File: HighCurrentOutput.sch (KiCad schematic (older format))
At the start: 8 parts, among them J10 OUT 1, Q1 SISA88DN or similar

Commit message: preliminary placement done
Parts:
- J10: footprint Connector_Molex:Molex_Nano-Fit_105313-xx02_1x02_P2.50mm_Horizontal -> TXV_LIB:Molex_Nano-Fit_105313-xx02_1x02_P2.50mm_Horizontal
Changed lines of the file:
@@
 F 0 "J20" H 6105 3317 50  0000 L CNN
 F 1 "OUT 1" H 6105 3226 50  0000 L CNN
-F 2 "Connector_Molex:Molex_Nano-Fit_105313-xx02_1x02_P2.50mm_Horizontal" H 6025 3325 50  0001 C CNN
+F 2 "TXV_LIB:Molex_Nano-Fit_105313-xx02_1x02_P2.50mm_Horizontal" H 6025 3325 50  0001 C CNN
 F 3 "" H 6025 3325 50  0001 C CNN
 F 4 "" H 6025 3325 50  0001 C CNN "Male Mate"

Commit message: changed form factor to better fit into uHb engine section
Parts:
- J10: footprint TXV_LIB:Molex_Nano-Fit_105313-xx02_1x02_P2.50mm_Horizontal -> TXV_LIB:Molex_Nano-Fit_105309-xx02_1x02_P2.50mm_Vertical
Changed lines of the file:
@@
 F 0 "J20" H 6105 3317 50  0000 L CNN
 F 1 "OUT 1" H 6105 3226 50  0000 L CNN
-F 2 "TXV_LIB:Molex_Nano-Fit_105313-xx02_1x02_P2.50mm_Horizontal" H 6025 3325 50  0001 C CNN
+F 2 "TXV_LIB:Molex_Nano-Fit_105309-xx02_1x02_P2.50mm_Vertical" H 6025 3325 50  0001 C CNN
 F 3 "" H 6025 3325 50  0001 C CNN
 F 4 "" H 6025 3325 50  0001 C CNN "Male Mate"

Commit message: many small changes, before removing servo buck converter
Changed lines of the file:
@@
 AR Path="/636FF559/637A9A68" Ref="J10"  Part="1"
 AR Path="/64079439/637A9A68" Ref="J20"  Part="1"
-F 0 "J20" H 6105 3317 50  0000 L CNN
+F 0 "J10" H 6105 3317 50  0000 L CNN
 F 1 "OUT 1" H 6105 3226 50  0000 L CNN
 F 2 "TXV_LIB:Molex_Nano-Fit_105309-xx02_1x02_P2.50mm_Vertical" H 6025 3325 50  0001 C CNN
@@
 AR Path="/636FF559/637A9A72" Ref="#PWR0119"  Part="1"
 AR Path="/64079439/637A9A72" Ref="#PWR0176"  Part="1"
-F 0 "#PWR0176" H 5800 3075 50  0001 C CNN
+F 0 "#PWR0119" H 5800 3075 50  0001 C CNN
 F 1 "+12V" H 5800 3375 50  0000 C CNN
 F 2 "" H 5800 3225 50  0001 C CNN
@@
 AR Path="/636FF559/637A9A79" Ref="D7"  Part="1"
 AR Path="/64079439/637A9A79" Ref="D10"  Part="1"
-F 0 "D10" V 5650 3575 50  0000 R CNN
+F 0 "D7" V 5650 3575 50  0000 R CNN
 F 1 "Shottky" V 5725 3700 50  0000 R CNN
 F 2 "Diode_SMD:D_SOD-123F" V 5700 3375 50  0001 C CNN
@@
 AR Path="/636FF559/637A9A88" Ref="R29"  Part="1"
 AR Path="/64079439/637A9A88" Ref="R58"  Part="1"
-F 0 "R58" H 5175 3825 50  0000 R CNN
+F 0 "R29" H 5175 3825 50  0000 R CNN
 F 1 "9k1" H 5175 3900 50  0000 R CNN
 F 2 "Resistor_SMD:R_0603_1608Metric" H 5225 3850 50  0001 C CNN
@@
 AR Path="/636FF559/637A9A8F" Ref="#PWR0120"  Part="1"
 AR Path="/64079439/637A9A8F" Ref="#PWR0177"  Part="1"
-F 0 "#PWR0177" H 5800 3950 50  0001 C CNN
+F 0 "#PWR0120" H 5800 3950 50  0001 C CNN
 F 1 "GND" H 5800 4050 50  0000 C CNN
 F 2 "" H 5800 4200 50  0001 C CNN
@@
 AR Path="/636FF559/637A9A95" Ref="R30"  Part="1"
 AR Path="/64079439/637A9A95" Ref="R59"  Part="1"
-F 0 "R59" V 5525 3725 50  0000 C CNN
+F 0 "R30" V 5525 3725 50  0000 C CNN
 F 1 "120" V 5450 3725 50  0000 C CNN
 F 2 "Resistor_SMD:R_0603_1608Metric" H 5375 3725 50  0001 C CNN
@@
 AR Path="/636FF559/637A9A9F" Ref="R31"  Part="1"
 AR Path="/64079439/637A9A9F" Ref="R60"  Part="1"
-F 0 "R60" H 5600 4125 50  0000 L CNN
+F 0 "R31" H 5600 4125 50  0000 L CNN
 F 1 "10m 1W" H 5450 4025 50  0000 L CNN
 F 2 "Resistor_SMD:R_1206_3216Metric" H 5800 4075 50  0001 C CNN
@@
 AR Path="/636FF559/637A9AAA" Ref="D6"  Part="1"
 AR Path="/64079439/637A9AAA" Ref="D9"  Part="1"
-F 0 "D9" V 5100 4275 50  0000 R CNN
+F 0 "D6" V 5100 4275 50  0000 R CNN
 F 1 "OUT 1" V 5025 4375 50  0000 R CNN
 F 2 "LED_SMD:LED_0603_1608Metric" V 5075 4075 50  0001 C CNN
@@
 AR Path="/636FF559/637A9AB0" Ref="#PWR0121"  Part="1"
 AR Path="/64079439/637A9AB0" Ref="#PWR0178"  Part="1"
-F 0 "#PWR0178" H 5075 3950 50  0001 C CNN
+F 0 "#PWR0121" H 5075 3950 50  0001 C CNN
 F 1 "GND" H 5075 4050 50  0000 C CNN
 F 2 "" H 5075 4200 50  0001 C CNN
@@
 AR Path="/636FF559/637A9ABC" Ref="#PWR0122"  Part="1"
 AR Path="/64079439/637A9ABC" Ref="#PWR0179"  Part="1"
-F 0 "#PWR0179" H 5225 3725 50  0001 C CNN
+F 0 "#PWR0122" H 5225 3725 50  0001 C CNN
 F 1 "GND" H 5225 3825 50  0000 C CNN
 F 2 "" H 5225 3975 50  0001 C CNN
@@
 AR Path="/636FF559/637A9AC2" Ref="R28"  Part="1"
 AR Path="/64079439/637A9AC2" Ref="R57"  Part="1"
-F 0 "R57" H 4950 3875 50  0000 C CNN
+F 0 "R28" H 4950 3875 50  0000 C CNN
 F 1 "120" H 4950 3800 50  0000 C CNN
 F 2 "Resistor_SMD:R_0603_1608Metric" H 5075 3850 50  0001 C CNN
@@
 AR Path="/636FF559/637A9AC9" Ref="Q1"  Part="1"
 AR Path="/64079439/637A9AC9" Ref="Q2"  Part="1"
-F 0 "Q2" H 5905 3771 50  0000 L CNN
+F 0 "Q1" H 5905 3771 50  0000 L CNN
 F 1 "SISA88DN or similar" H 5905 3680 50  0000 L CNN
 F 2 "TXV_LIB:PowerPAK_1212-8" H 5900 3825 50  0001 C CNN

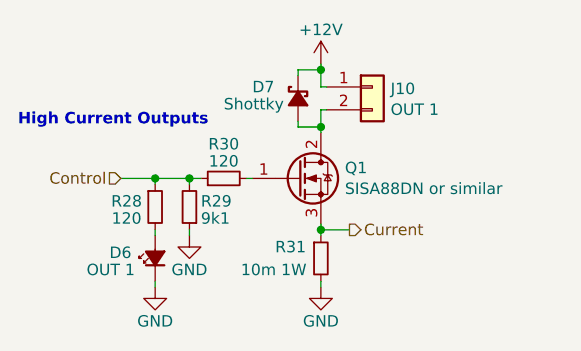
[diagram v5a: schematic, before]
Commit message: fixed net names
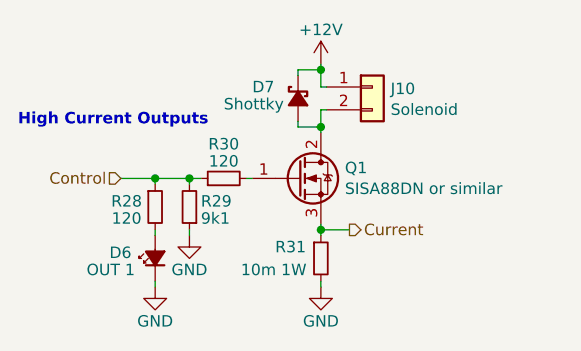
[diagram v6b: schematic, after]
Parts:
- J10: value OUT 1 -> Solenoid
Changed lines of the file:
@@
 AR Path="/64079439/637A9A68" Ref="J20"  Part="1"
 F 0 "J10" H 6105 3317 50  0000 L CNN
-F 1 "OUT 1" H 6105 3226 50  0000 L CNN
+F 1 "Solenoid" H 6105 3226 50  0000 L CNN
 F 2 "TXV_LIB:Molex_Nano-Fit_105309-xx02_1x02_P2.50mm_Vertical" H 6025 3325 50  0001 C CNN
 F 3 "" H 6025 3325 50  0001 C CNN
@@
 AR Path="/636FF559/637A9A72" Ref="#PWR0119"  Part="1"
 AR Path="/64079439/637A9A72" Ref="#PWR0176"  Part="1"
-F 0 "#PWR0119" H 5800 3075 50  0001 C CNN
+F 0 "#PWR0176" H 5800 3075 50  0001 C CNN
 F 1 "+12V" H 5800 3375 50  0000 C CNN
 F 2 "" H 5800 3225 50  0001 C CNN
@@
 AR Path="/636FF559/637A9A8F" Ref="#PWR0120"  Part="1"
 AR Path="/64079439/637A9A8F" Ref="#PWR0177"  Part="1"
-F 0 "#PWR0120" H 5800 3950 50  0001 C CNN
+F 0 "#PWR0177" H 5800 3950 50  0001 C CNN
 F 1 "GND" H 5800 4050 50  0000 C CNN
 F 2 "" H 5800 4200 50  0001 C CNN
@@
 AR Path="/636FF559/637A9AB0" Ref="#PWR0121"  Part="1"
 AR Path="/64079439/637A9AB0" Ref="#PWR0178"  Part="1"
-F 0 "#PWR0121" H 5075 3950 50  0001 C CNN
+F 0 "#PWR0178" H 5075 3950 50  0001 C CNN
 F 1 "GND" H 5075 4050 50  0000 C CNN
 F 2 "" H 5075 4200 50  0001 C CNN
@@
 AR Path="/636FF559/637A9ABC" Ref="#PWR0122"  Part="1"
 AR Path="/64079439/637A9ABC" Ref="#PWR0179"  Part="1"
-F 0 "#PWR0122" H 5225 3725 50  0001 C CNN
+F 0 "#PWR0179" H 5225 3725 50  0001 C CNN
 F 1 "GND" H 5225 3825 50  0000 C CNN
 F 2 "" H 5225 3975 50  0001 C CNN

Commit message: schematic done, preliminary placement done
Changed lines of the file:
@@
 $Descr A4 11693 8268
 encoding utf-8
-Sheet 5 18
+Sheet 13 18
 Title ""
 Date ""
@@
 AR Path="/636FF559/637A9A68" Ref="J10"  Part="1"
 AR Path="/64079439/637A9A68" Ref="J20"  Part="1"
-F 0 "J10" H 6105 3317 50  0000 L CNN
+F 0 "J20" H 6105 3317 50  0000 L CNN
 F 1 "Solenoid" H 6105 3226 50  0000 L CNN
 F 2 "TXV_LIB:Molex_Nano-Fit_105309-xx02_1x02_P2.50mm_Vertical" H 6025 3325 50  0001 C CNN
@@
 AR Path="/636FF559/637A9A79" Ref="D7"  Part="1"
 AR Path="/64079439/637A9A79" Ref="D10"  Part="1"
-F 0 "D7" V 5650 3575 50  0000 R CNN
+F 0 "D10" V 5650 3575 50  0000 R CNN
 F 1 "Shottky" V 5725 3700 50  0000 R CNN
 F 2 "Diode_SMD:D_SOD-123F" V 5700 3375 50  0001 C CNN
@@
 AR Path="/636FF559/637A9A88" Ref="R29"  Part="1"
 AR Path="/64079439/637A9A88" Ref="R58"  Part="1"
-F 0 "R29" H 5175 3825 50  0000 R CNN
+F 0 "R58" H 5175 3825 50  0000 R CNN
 F 1 "9k1" H 5175 3900 50  0000 R CNN
 F 2 "Resistor_SMD:R_0603_1608Metric" H 5225 3850 50  0001 C CNN
@@
 AR Path="/636FF559/637A9A95" Ref="R30"  Part="1"
 AR Path="/64079439/637A9A95" Ref="R59"  Part="1"
-F 0 "R30" V 5525 3725 50  0000 C CNN
+F 0 "R59" V 5525 3725 50  0000 C CNN
 F 1 "120" V 5450 3725 50  0000 C CNN
 F 2 "Resistor_SMD:R_0603_1608Metric" H 5375 3725 50  0001 C CNN
@@
 AR Path="/636FF559/637A9A9F" Ref="R31"  Part="1"
 AR Path="/64079439/637A9A9F" Ref="R60"  Part="1"
-F 0 "R31" H 5600 4125 50  0000 L CNN
+F 0 "R60" H 5600 4125 50  0000 L CNN
 F 1 "10m 1W" H 5450 4025 50  0000 L CNN
 F 2 "Resistor_SMD:R_1206_3216Metric" H 5800 4075 50  0001 C CNN
@@
 AR Path="/636FF559/637A9AAA" Ref="D6"  Part="1"
 AR Path="/64079439/637A9AAA" Ref="D9"  Part="1"
-F 0 "D6" V 5100 4275 50  0000 R CNN
+F 0 "D9" V 5100 4275 50  0000 R CNN
 F 1 "OUT 1" V 5025 4375 50  0000 R CNN
 F 2 "LED_SMD:LED_0603_1608Metric" V 5075 4075 50  0001 C CNN
@@
 AR Path="/636FF559/637A9AC2" Ref="R28"  Part="1"
 AR Path="/64079439/637A9AC2" Ref="R57"  Part="1"
-F 0 "R28" H 4950 3875 50  0000 C CNN
+F 0 "R57" H 4950 3875 50  0000 C CNN
 F 1 "120" H 4950 3800 50  0000 C CNN
 F 2 "Resistor_SMD:R_0603_1608Metric" H 5075 3850 50  0001 C CNN
@@
 AR Path="/636FF559/637A9AC9" Ref="Q1"  Part="1"
 AR Path="/64079439/637A9AC9" Ref="Q2"  Part="1"
-F 0 "Q1" H 5905 3771 50  0000 L CNN
+F 0 "Q2" H 5905 3771 50  0000 L CNN
 F 1 "SISA88DN or similar" H 5905 3680 50  0000 L CNN
 F 2 "TXV_LIB:PowerPAK_1212-8" H 5900 3825 50  0001 C CNN

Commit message: some more small changes
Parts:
- R29: value 9k1 -> 10k
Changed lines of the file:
@@
 $Descr A4 11693 8268
 encoding utf-8
-Sheet 13 18
+Sheet 5 18
 Title ""
 Date ""
@@
 AR Path="/636FF559/637A9A68" Ref="J10"  Part="1"
 AR Path="/64079439/637A9A68" Ref="J20"  Part="1"
-F 0 "J20" H 6105 3317 50  0000 L CNN
+F 0 "J10" H 6105 3317 50  0000 L CNN
 F 1 "Solenoid" H 6105 3226 50  0000 L CNN
 F 2 "TXV_LIB:Molex_Nano-Fit_105309-xx02_1x02_P2.50mm_Vertical" H 6025 3325 50  0001 C CNN
@@
 AR Path="/636FF559/637A9A79" Ref="D7"  Part="1"
 AR Path="/64079439/637A9A79" Ref="D10"  Part="1"
-F 0 "D10" V 5650 3575 50  0000 R CNN
+F 0 "D7" V 5650 3575 50  0000 R CNN
 F 1 "Shottky" V 5725 3700 50  0000 R CNN
 F 2 "Diode_SMD:D_SOD-123F" V 5700 3375 50  0001 C CNN
@@
 AR Path="/636FF559/637A9A88" Ref="R29"  Part="1"
 AR Path="/64079439/637A9A88" Ref="R58"  Part="1"
-F 0 "R58" H 5175 3825 50  0000 R CNN
-F 1 "9k1" H 5175 3900 50  0000 R CNN
+F 0 "R29" H 5175 3825 50  0000 R CNN
+F 1 "10k" H 5175 3900 50  0000 R CNN
 F 2 "Resistor_SMD:R_0603_1608Metric" H 5225 3850 50  0001 C CNN
 F 3 "~" H 5225 3850 50  0001 C CNN
@@
 AR Path="/636FF559/637A9A95" Ref="R30"  Part="1"
 AR Path="/64079439/637A9A95" Ref="R59"  Part="1"
-F 0 "R59" V 5525 3725 50  0000 C CNN
+F 0 "R30" V 5525 3725 50  0000 C CNN
 F 1 "120" V 5450 3725 50  0000 C CNN
 F 2 "Resistor_SMD:R_0603_1608Metric" H 5375 3725 50  0001 C CNN
@@
 AR Path="/636FF559/637A9A9F" Ref="R31"  Part="1"
 AR Path="/64079439/637A9A9F" Ref="R60"  Part="1"
-F 0 "R60" H 5600 4125 50  0000 L CNN
+F 0 "R31" H 5600 4125 50  0000 L CNN
 F 1 "10m 1W" H 5450 4025 50  0000 L CNN
 F 2 "Resistor_SMD:R_1206_3216Metric" H 5800 4075 50  0001 C CNN
@@
 AR Path="/636FF559/637A9AAA" Ref="D6"  Part="1"
 AR Path="/64079439/637A9AAA" Ref="D9"  Part="1"
-F 0 "D9" V 5100 4275 50  0000 R CNN
+F 0 "D6" V 5100 4275 50  0000 R CNN
 F 1 "OUT 1" V 5025 4375 50  0000 R CNN
 F 2 "LED_SMD:LED_0603_1608Metric" V 5075 4075 50  0001 C CNN
@@
 AR Path="/636FF559/637A9AC2" Ref="R28"  Part="1"
 AR Path="/64079439/637A9AC2" Ref="R57"  Part="1"
-F 0 "R57" H 4950 3875 50  0000 C CNN
+F 0 "R28" H 4950 3875 50  0000 C CNN
 F 1 "120" H 4950 3800 50  0000 C CNN
 F 2 "Resistor_SMD:R_0603_1608Metric" H 5075 3850 50  0001 C CNN
@@
 AR Path="/636FF559/637A9AC9" Ref="Q1"  Part="1"
 AR Path="/64079439/637A9AC9" Ref="Q2"  Part="1"
-F 0 "Q2" H 5905 3771 50  0000 L CNN
+F 0 "Q1" H 5905 3771 50  0000 L CNN
 F 1 "SISA88DN or similar" H 5905 3680 50  0000 L CNN
 F 2 "TXV_LIB:PowerPAK_1212-8" H 5900 3825 50  0001 C CNN
